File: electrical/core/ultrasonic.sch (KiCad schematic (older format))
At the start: 7 parts, among them J4 Conn_01x04_Male, Q5 AO3400, Q6 AO3400

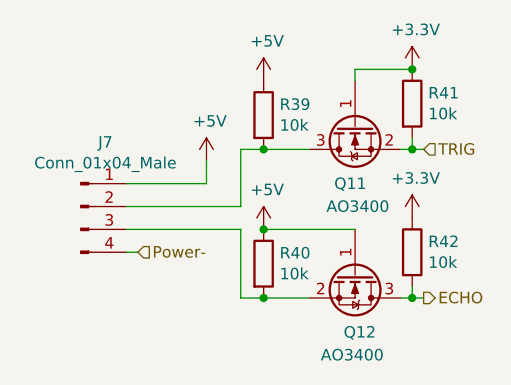
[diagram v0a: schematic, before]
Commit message: Make Dora have 4 motors
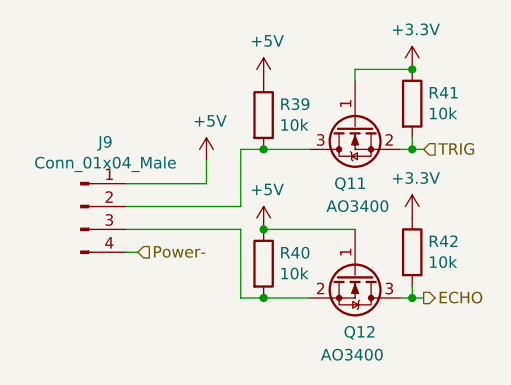
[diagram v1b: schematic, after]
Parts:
- renumbered J4 to J6
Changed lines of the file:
@@
 $Descr A4 11693 8268
 encoding utf-8
-Sheet 11 12
+Sheet 11 15
 Title ""
 Date ""
@@
 P 4650 3750
 AR Path="/5D1373A3/5DB4719C" Ref="J?"  Part="1"
-AR Path="/5D1373A3/5DB42710/5DB4719C" Ref="J4"  Part="1"
+AR Path="/5D1373A3/5DB42710/5DB4719C" Ref="J6"  Part="1"
 AR Path="/5D1373A3/5DBA0DBB/5DB4719C" Ref="J?"  Part="1"
 AR Path="/5D1373A3/5DBA1C1E/5DB4719C" Ref="J?"  Part="1"
@@
 AR Path="/5D1373A3/5DBA7DAA/5DB4719C" Ref="J?"  Part="1"
 AR Path="/5D1373A3/5DBA7DAF/5DB4719C" Ref="J?"  Part="1"
-AR Path="/5D1373A3/5E6481EF/5DB4719C" Ref="J5"  Part="1"
-AR Path="/5D1373A3/5E650C4B/5DB4719C" Ref="J6"  Part="1"
-AR Path="/5D1373A3/5E652B60/5DB4719C" Ref="J7"  Part="1"
-F 0 "J7" H 4758 4031 50  0000 C CNN
+AR Path="/5D1373A3/5E6481EF/5DB4719C" Ref="J7"  Part="1"
+AR Path="/5D1373A3/5E650C4B/5DB4719C" Ref="J8"  Part="1"
+AR Path="/5D1373A3/5E652B60/5DB4719C" Ref="J9"  Part="1"
+F 0 "J9" H 4758 4031 50  0000 C CNN
 F 1 "Conn_01x04_Male" H 4758 3940 50  0000 C CNN
 F 2 "Connector_PinHeader_2.54mm:PinHeader_1x04_P2.54mm_Vertical" H 4650 3750 50  0001 C CNN
@@
 P 5200 3550
 AR Path="/5D1373A3/5DB471A5" Ref="#PWR?"  Part="1"
-AR Path="/5D1373A3/5DB42710/5DB471A5" Ref="#PWR070"  Part="1"
+AR Path="/5D1373A3/5DB42710/5DB471A5" Ref="#PWR074"  Part="1"
 AR Path="/5D1373A3/5DBA0DBB/5DB471A5" Ref="#PWR?"  Part="1"
 AR Path="/5D1373A3/5DBA1C1E/5DB471A5" Ref="#PWR?"  Part="1"
@@
 AR Path="/5D1373A3/5DBA7DAA/5DB471A5" Ref="#PWR?"  Part="1"
 AR Path="/5D1373A3/5DBA7DAF/5DB471A5" Ref="#PWR?"  Part="1"
-AR Path="/5D1373A3/5E6481EF/5DB471A5" Ref="#PWR075"  Part="1"
-AR Path="/5D1373A3/5E650C4B/5DB471A5" Ref="#PWR080"  Part="1"
-AR Path="/5D1373A3/5E652B60/5DB471A5" Ref="#PWR085"  Part="1"
-F 0 "#PWR085" H 5200 3400 50  0001 C CNN
+AR Path="/5D1373A3/5E6481EF/5DB471A5" Ref="#PWR079"  Part="1"
+AR Path="/5D1373A3/5E650C4B/5DB471A5" Ref="#PWR084"  Part="1"
+AR Path="/5D1373A3/5E652B60/5DB471A5" Ref="#PWR089"  Part="1"
+F 0 "#PWR089" H 5200 3400 50  0001 C CNN
 F 1 "+5V" H 5215 3723 50  0000 C CNN
 F 2 "" H 5200 3550 50  0001 C CNN
@@
 TRIG
 $Comp
-L power:+5V #PWR071
+L power:+5V #PWR075
 U 1 1 5DB5AAB6
 P 5450 3200
-AR Path="/5D1373A3/5DB42710/5DB5AAB6" Ref="#PWR071"  Part="1"
+AR Path="/5D1373A3/5DB42710/5DB5AAB6" Ref="#PWR075"  Part="1"
 AR Path="/5D1373A3/5DBA0DBB/5DB5AAB6" Ref="#PWR?"  Part="1"
 AR Path="/5D1373A3/5DBA1C1E/5DB5AAB6" Ref="#PWR?"  Part="1"
@@
 AR Path="/5D1373A3/5DBA7DAA/5DB5AAB6" Ref="#PWR?"  Part="1"
 AR Path="/5D1373A3/5DBA7DAF/5DB5AAB6" Ref="#PWR?"  Part="1"
-AR Path="/5D1373A3/5E6481EF/5DB5AAB6" Ref="#PWR076"  Part="1"
-AR Path="/5D1373A3/5E650C4B/5DB5AAB6" Ref="#PWR081"  Part="1"
-AR Path="/5D1373A3/5E652B60/5DB5AAB6" Ref="#PWR086"  Part="1"
-F 0 "#PWR086" H 5450 3050 50  0001 C CNN
+AR Path="/5D1373A3/5E6481EF/5DB5AAB6" Ref="#PWR080"  Part="1"
+AR Path="/5D1373A3/5E650C4B/5DB5AAB6" Ref="#PWR085"  Part="1"
+AR Path="/5D1373A3/5E652B60/5DB5AAB6" Ref="#PWR090"  Part="1"
+F 0 "#PWR090" H 5450 3050 50  0001 C CNN
 F 1 "+5V" H 5465 3373 50  0000 C CNN
 F 2 "" H 5450 3200 50  0001 C CNN
@@
 ECHO
 $Comp
-L power:+3.3V #PWR073
+L power:+3.3V #PWR077
 U 1 1 5DB62EEB
 P 6100 3150
-AR Path="/5D1373A3/5DB42710/5DB62EEB" Ref="#PWR073"  Part="1"
+AR Path="/5D1373A3/5DB42710/5DB62EEB" Ref="#PWR077"  Part="1"
 AR Path="/5D1373A3/5DBA0DBB/5DB62EEB" Ref="#PWR?"  Part="1"
 AR Path="/5D1373A3/5DBA1C1E/5DB62EEB" Ref="#PWR?"  Part="1"
@@
 AR Path="/5D1373A3/5DBA7DAA/5DB62EEB" Ref="#PWR?"  Part="1"
 AR Path="/5D1373A3/5DBA7DAF/5DB62EEB" Ref="#PWR?"  Part="1"
-AR Path="/5D1373A3/5E6481EF/5DB62EEB" Ref="#PWR078"  Part="1"
-AR Path="/5D1373A3/5E650C4B/5DB62EEB" Ref="#PWR083"  Part="1"
-AR Path="/5D1373A3/5E652B60/5DB62EEB" Ref="#PWR088"  Part="1"
-F 0 "#PWR088" H 6100 3000 50  0001 C CNN
+AR Path="/5D1373A3/5E6481EF/5DB62EEB" Ref="#PWR082"  Part="1"
+AR Path="/5D1373A3/5E650C4B/5DB62EEB" Ref="#PWR087"  Part="1"
+AR Path="/5D1373A3/5E652B60/5DB62EEB" Ref="#PWR092"  Part="1"
+F 0 "#PWR092" H 6100 3000 50  0001 C CNN
 F 1 "+3.3V" H 6115 3323 50  0000 C CNN
 F 2 "" H 6100 3150 50  0001 C CNN
@@
 	5450 3500 5650 3500
 $Comp
-L power:+5V #PWR072
+L power:+5V #PWR076
 U 1 1 5E680E9A
 P 5450 3850
-AR Path="/5D1373A3/5DB42710/5E680E9A" Ref="#PWR072"  Part="1"
+AR Path="/5D1373A3/5DB42710/5E680E9A" Ref="#PWR076"  Part="1"
 AR Path="/5D1373A3/5DBA0DBB/5E680E9A" Ref="#PWR?"  Part="1"
 AR Path="/5D1373A3/5DBA1C1E/5E680E9A" Ref="#PWR?"  Part="1"
@@
 AR Path="/5D1373A3/5DBA7DAA/5E680E9A" Ref="#PWR?"  Part="1"
 AR Path="/5D1373A3/5DBA7DAF/5E680E9A" Ref="#PWR?"  Part="1"
-AR Path="/5D1373A3/5E6481EF/5E680E9A" Ref="#PWR077"  Part="1"
-AR Path="/5D1373A3/5E650C4B/5E680E9A" Ref="#PWR082"  Part="1"
-AR Path="/5D1373A3/5E652B60/5E680E9A" Ref="#PWR087"  Part="1"
-F 0 "#PWR087" H 5450 3700 50  0001 C CNN
+AR Path="/5D1373A3/5E6481EF/5E680E9A" Ref="#PWR081"  Part="1"
+AR Path="/5D1373A3/5E650C4B/5E680E9A" Ref="#PWR086"  Part="1"
+AR Path="/5D1373A3/5E652B60/5E680E9A" Ref="#PWR091"  Part="1"
+F 0 "#PWR091" H 5450 3700 50  0001 C CNN
 F 1 "+5V" H 5465 4023 50  0000 C CNN
 F 2 "" H 5450 3850 50  0001 C CNN
@@
 $EndComp
 $Comp
-L power:+3.3V #PWR074
+L power:+3.3V #PWR078
 U 1 1 5E68391F
 P 6100 3800
-AR Path="/5D1373A3/5DB42710/5E68391F" Ref="#PWR074"  Part="1"
+AR Path="/5D1373A3/5DB42710/5E68391F" Ref="#PWR078"  Part="1"
 AR Path="/5D1373A3/5DBA0DBB/5E68391F" Ref="#PWR?"  Part="1"
 AR Path="/5D1373A3/5DBA1C1E/5E68391F" Ref="#PWR?"  Part="1"
@@
 AR Path="/5D1373A3/5DBA7DAA/5E68391F" Ref="#PWR?"  Part="1"
 AR Path="/5D1373A3/5DBA7DAF/5E68391F" Ref="#PWR?"  Part="1"
-AR Path="/5D1373A3/5E6481EF/5E68391F" Ref="#PWR079"  Part="1"
-AR Path="/5D1373A3/5E650C4B/5E68391F" Ref="#PWR084"  Part="1"
-AR Path="/5D1373A3/5E652B60/5E68391F" Ref="#PWR089"  Part="1"
-F 0 "#PWR089" H 6100 3650 50  0001 C CNN
+AR Path="/5D1373A3/5E6481EF/5E68391F" Ref="#PWR083"  Part="1"
+AR Path="/5D1373A3/5E650C4B/5E68391F" Ref="#PWR088"  Part="1"
+AR Path="/5D1373A3/5E652B60/5E68391F" Ref="#PWR093"  Part="1"
+F 0 "#PWR093" H 6100 3650 50  0001 C CNN
 F 1 "+3.3V" H 6115 3973 50  0000 C CNN
 F 2 "" H 6100 3800 50  0001 C CNN
